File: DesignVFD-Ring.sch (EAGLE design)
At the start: 30 parts, among them IC1 LMR64010XMF/NOPB, IC2 LM340S-05, U1 MAX6920AWP+, U2 LM1084IS-5.0, U3 TPS76325DBVT

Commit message: Initial layout complete
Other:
- moved on the sheet: JP1
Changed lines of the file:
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@@
 <sheet>
 <plain>
-<text x="60.96" y="101.6" size="1.778" layer="91">Ribbon Cable for Ring</text>
+<text x="7.62" y="129.54" size="1.778" layer="91">Ribbon Cable for Ring</text>
 <text x="-73.66" y="246.38" size="6.4516" layer="91">TODO sort Caps</text>
 <text x="73.66" y="332.74" size="6.4516" layer="91">Batt to 12V</text>
@@
 </plain>
 <instances>
-<instance part="JP1" gate="A" x="76.2" y="93.98" smashed="yes" rot="R90">
-<attribute name="NAME" x="65.405" y="87.63" size="1.778" layer="95"/>
-<attribute name="VALUE" x="86.36" y="87.63" size="1.778" layer="96" rot="R90"/>
+<instance part="JP1" gate="A" x="22.86" y="121.92" smashed="yes" rot="R90">
+<attribute name="NAME" x="12.065" y="115.57" size="1.778" layer="95"/>
+<attribute name="VALUE" x="33.02" y="115.57" size="1.778" layer="96" rot="R90"/>
 </instance>
 <instance part="IC1" gate="G$1" x="17.78" y="182.88" smashed="yes">
@@
 <segment>
 <pinref part="JP1" gate="A" pin="1"/>
-<wire x1="68.58" y1="91.44" x2="68.58" y2="76.2" width="0.1524" layer="91"/>
-<label x="68.58" y="76.2" size="1.778" layer="95" rot="R90"/>
+<wire x1="15.24" y1="119.38" x2="15.24" y2="104.14" width="0.1524" layer="91"/>
+<label x="15.24" y="104.14" size="1.778" layer="95" rot="R90"/>
 </segment>
 <segment>
 <pinref part="JP1" gate="A" pin="3"/>
-<wire x1="73.66" y1="91.44" x2="73.66" y2="76.2" width="0.1524" layer="91"/>
-<label x="73.66" y="76.2" size="1.778" layer="95" rot="R90"/>
+<wire x1="20.32" y1="119.38" x2="20.32" y2="104.14" width="0.1524" layer="91"/>
+<label x="20.32" y="104.14" size="1.778" layer="95" rot="R90"/>
 </segment>
 <segment>
 <pinref part="JP1" gate="A" pin="5"/>
-<wire x1="78.74" y1="91.44" x2="78.74" y2="76.2" width="0.1524" layer="91"/>
-<label x="78.74" y="76.2" size="1.778" layer="95" rot="R90"/>
+<wire x1="25.4" y1="119.38" x2="25.4" y2="104.14" width="0.1524" layer="91"/>
+<label x="25.4" y="104.14" size="1.778" layer="95" rot="R90"/>
 </segment>
 <segment>
 <pinref part="JP1" gate="A" pin="7"/>
-<wire x1="83.82" y1="91.44" x2="83.82" y2="76.2" width="0.1524" layer="91"/>
-<label x="83.82" y="76.2" size="1.778" layer="95" rot="R90"/>
+<wire x1="30.48" y1="119.38" x2="30.48" y2="104.14" width="0.1524" layer="91"/>
+<label x="30.48" y="104.14" size="1.778" layer="95" rot="R90"/>
 </segment>
 <segment>
@@
 <segment>
 <pinref part="JP1" gate="A" pin="2"/>
-<wire x1="71.12" y1="91.44" x2="71.12" y2="76.2" width="0.1524" layer="91"/>
-<label x="71.12" y="76.2" size="1.778" layer="95" rot="R90"/>
+<wire x1="17.78" y1="119.38" x2="17.78" y2="104.14" width="0.1524" layer="91"/>
+<label x="17.78" y="104.14" size="1.778" layer="95" rot="R90"/>
 </segment>
 <segment>
@@
 <segment>
 <pinref part="JP1" gate="A" pin="4"/>
-<wire x1="76.2" y1="91.44" x2="76.2" y2="76.2" width="0.1524" layer="91"/>
-<label x="76.2" y="76.2" size="1.778" layer="95" rot="R90"/>
+<wire x1="22.86" y1="119.38" x2="22.86" y2="104.14" width="0.1524" layer="91"/>
+<label x="22.86" y="104.14" size="1.778" layer="95" rot="R90"/>
 </segment>
 <segment>
@@
 <segment>
 <pinref part="JP1" gate="A" pin="6"/>
-<wire x1="81.28" y1="91.44" x2="81.28" y2="76.2" width="0.1524" layer="91"/>
-<label x="81.28" y="76.2" size="1.778" layer="95" rot="R90"/>
-</segment>
-<segment>
+<wire x1="27.94" y1="119.38" x2="27.94" y2="104.14" width="0.1524" layer="91"/>
+<label x="27.94" y="104.14" size="1.778" layer="95" rot="R90"/>
+</segment>
+<segment>

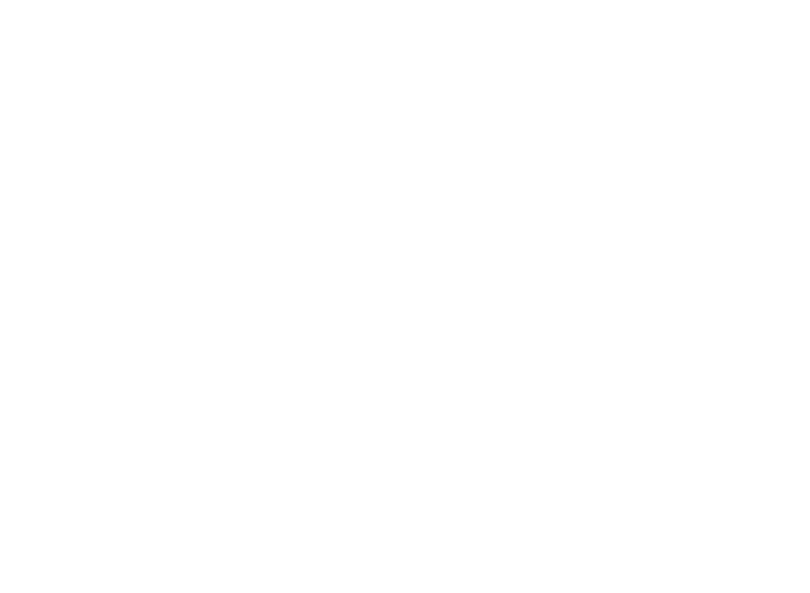
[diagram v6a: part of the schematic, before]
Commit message: added lumini ring
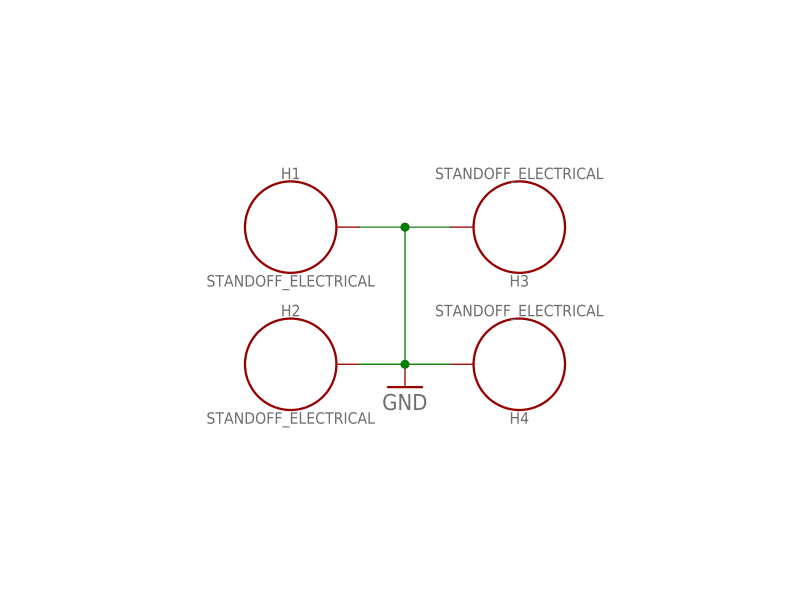
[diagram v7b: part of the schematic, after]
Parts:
- added H1, H2, H3, H4: STANDOFF_ELECTRICAL, SparkFun-Hardware:STANDOFF_ELECTRICAL
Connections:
- net GND: now also H1.P$1, H2.P$1, H3.P$1, H4.P$1
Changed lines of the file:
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@@
 <layer number="112" name="tSilk" color="7" fill="1" visible="no" active="yes"/>
 <layer number="113" name="ReferenceLS" color="7" fill="1" visible="no" active="no"/>
+<layer number="114" name="Badge_Outline" color="7" fill="1" visible="no" active="no"/>
+<layer number="115" name="ReferenceISLANDS" color="7" fill="1" visible="no" active="no"/>
 <layer number="116" name="Patch_BOT" color="9" fill="4" visible="no" active="yes"/>
 <layer number="118" name="Rect_Pads" color="7" fill="1" visible="no" active="no"/>
@@
 <part name="+3V4" library="supply1" library_urn="urn:adsk.eagle:library:371" deviceset="+3V3" device=""/>
 <part name="P+10" library="supply1" library_urn="urn:adsk.eagle:library:371" deviceset="+5V" device=""/>
+<part name="H1" library="SparkFun-Hardware" deviceset="STANDOFF_ELECTRICAL" device=""/>
+<part name="H2" library="SparkFun-Hardware" deviceset="STANDOFF_ELECTRICAL" device=""/>
+<part name="H3" library="SparkFun-Hardware" deviceset="STANDOFF_ELECTRICAL" device=""/>
+<part name="H4" library="SparkFun-Hardware" deviceset="STANDOFF_ELECTRICAL" device=""/>
+<part name="GND3" library="supply1" library_urn="urn:adsk.eagle:library:371" deviceset="GND" device=""/>
 </parts>
 <sheets>
@@
 <attribute name="VALUE" x="53.34" y="71.12" size="1.778" layer="96"/>
 </instance>
+<instance part="H1" gate="G$1" x="104.14" y="66.04" smashed="yes">
+<attribute name="NAME" x="104.14" y="71.374" size="1.27" layer="95" font="vector" align="bottom-center"/>
+<attribute name="VALUE" x="104.14" y="60.706" size="1.27" layer="96" font="vector" rot="R180" align="bottom-center"/>
+</instance>
+<instance part="H2" gate="G$1" x="104.14" y="50.8" smashed="yes">
+<attribute name="NAME" x="104.14" y="56.134" size="1.27" layer="95" font="vector" align="bottom-center"/>
+<attribute name="VALUE" x="104.14" y="45.466" size="1.27" layer="96" font="vector" rot="R180" align="bottom-center"/>
+</instance>
+<instance part="H3" gate="G$1" x="129.54" y="66.04" smashed="yes" rot="R180">
+<attribute name="NAME" x="129.54" y="60.706" size="1.27" layer="95" font="vector" rot="R180" align="bottom-center"/>
+<attribute name="VALUE" x="129.54" y="71.374" size="1.27" layer="96" font="vector" align="bottom-center"/>
+</instance>
+<instance part="H4" gate="G$1" x="129.54" y="50.8" smashed="yes" rot="R180">
+<attribute name="NAME" x="129.54" y="45.466" size="1.27" layer="95" font="vector" rot="R180" align="bottom-center"/>
+<attribute name="VALUE" x="129.54" y="56.134" size="1.27" layer="96" font="vector" align="bottom-center"/>
+</instance>
+<instance part="GND3" gate="1" x="116.84" y="48.26" smashed="yes">
+<attribute name="VALUE" x="114.3" y="45.72" size="1.778" layer="96"/>
+</instance>
 </instances>
 <busses>
@@
 <junction x="53.34" y="63.5"/>
 </segment>
+<segment>
+<pinref part="H1" gate="G$1" pin="P$1"/>
+<pinref part="H3" gate="G$1" pin="P$1"/>
+<wire x1="111.76" y1="66.04" x2="116.84" y2="66.04" width="0.1524" layer="91"/>
+<pinref part="H4" gate="G$1" pin="P$1"/>
+<pinref part="H2" gate="G$1" pin="P$1"/>
+<wire x1="116.84" y1="66.04" x2="121.92" y2="66.04" width="0.1524" layer="91"/>
+<wire x1="121.92" y1="50.8" x2="116.84" y2="50.8" width="0.1524" layer="91"/>
+<wire x1="116.84" y1="50.8" x2="111.76" y2="50.8" width="0.1524" layer="91"/>
+<wire x1="116.84" y1="66.04" x2="116.84" y2="50.8" width="0.1524" layer="91"/>
+<junction x="116.84" y="66.04"/>
+<junction x="116.84" y="50.8"/>
+<pinref part="GND3" gate="1" pin="GND"/>
+</segment>
 </net>

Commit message: about to repin IVL
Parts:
- removed H1, H2, H3, H4: STANDOFF_ELECTRICAL, SparkFun-Hardware:STANDOFF_ELECTRICAL
- added JP3: (no value), pinhead:PINHD-1X1
- added U$4: LUMINI3, FormE:LUMINI3
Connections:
- net +15V: now also JP3.1
- net GND: now also U$4.P$1; no longer H1.P$1, H2.P$1, H3.P$1, H4.P$1
- net T_CS2: now also U$3.3/CAN-TX/PWM; no longer U$3.5/PWM
- net T_MOSI2: now also U$3.5/PWM; no longer U$3.3/CAN-TX/PWM
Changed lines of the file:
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@@
 <part name="+3V4" library="supply1" library_urn="urn:adsk.eagle:library:371" deviceset="+3V3" device=""/>
 <part name="P+10" library="supply1" library_urn="urn:adsk.eagle:library:371" deviceset="+5V" device=""/>
-<part name="H1" library="SparkFun-Hardware" deviceset="STANDOFF_ELECTRICAL" device=""/>
-<part name="H2" library="SparkFun-Hardware" deviceset="STANDOFF_ELECTRICAL" device=""/>
-<part name="H3" library="SparkFun-Hardware" deviceset="STANDOFF_ELECTRICAL" device=""/>
-<part name="H4" library="SparkFun-Hardware" deviceset="STANDOFF_ELECTRICAL" device=""/>
 <part name="GND3" library="supply1" library_urn="urn:adsk.eagle:library:371" deviceset="GND" device=""/>
+<part name="U$4" library="FormE" deviceset="LUMINI3" device=""/>
+<part name="JP3" library="pinhead" library_urn="urn:adsk.eagle:library:325" deviceset="PINHD-1X1" device="" package3d_urn="urn:adsk.eagle:package:22485/2"/>
 </parts>
 <sheets>
@@
 <attribute name="VALUE" x="53.34" y="71.12" size="1.778" layer="96"/>
 </instance>
-<instance part="H1" gate="G$1" x="104.14" y="66.04" smashed="yes">
-<attribute name="NAME" x="104.14" y="71.374" size="1.27" layer="95" font="vector" align="bottom-center"/>
-<attribute name="VALUE" x="104.14" y="60.706" size="1.27" layer="96" font="vector" rot="R180" align="bottom-center"/>
-</instance>
-<instance part="H2" gate="G$1" x="104.14" y="50.8" smashed="yes">
-<attribute name="NAME" x="104.14" y="56.134" size="1.27" layer="95" font="vector" align="bottom-center"/>
-<attribute name="VALUE" x="104.14" y="45.466" size="1.27" layer="96" font="vector" rot="R180" align="bottom-center"/>
-</instance>
-<instance part="H3" gate="G$1" x="129.54" y="66.04" smashed="yes" rot="R180">
-<attribute name="NAME" x="129.54" y="60.706" size="1.27" layer="95" font="vector" rot="R180" align="bottom-center"/>
-<attribute name="VALUE" x="129.54" y="71.374" size="1.27" layer="96" font="vector" align="bottom-center"/>
-</instance>
-<instance part="H4" gate="G$1" x="129.54" y="50.8" smashed="yes" rot="R180">
-<attribute name="NAME" x="129.54" y="45.466" size="1.27" layer="95" font="vector" rot="R180" align="bottom-center"/>
-<attribute name="VALUE" x="129.54" y="56.134" size="1.27" layer="96" font="vector" align="bottom-center"/>
-</instance>
 <instance part="GND3" gate="1" x="116.84" y="48.26" smashed="yes">
 <attribute name="VALUE" x="114.3" y="45.72" size="1.778" layer="96"/>
+</instance>
+<instance part="U$4" gate="G$1" x="124.46" y="50.8" smashed="yes"/>
+<instance part="JP3" gate="G$1" x="-10.16" y="335.28" smashed="yes" rot="MR0">
+<attribute name="NAME" x="-3.81" y="338.455" size="1.778" layer="95" rot="MR0"/>
+<attribute name="VALUE" x="-3.81" y="330.2" size="1.778" layer="96" rot="MR0"/>
 </instance>
 </instances>
@@
 </segment>
 <segment>
-<pinref part="H1" gate="G$1" pin="P$1"/>
-<pinref part="H3" gate="G$1" pin="P$1"/>
-<wire x1="111.76" y1="66.04" x2="116.84" y2="66.04" width="0.1524" layer="91"/>
-<pinref part="H4" gate="G$1" pin="P$1"/>
-<pinref part="H2" gate="G$1" pin="P$1"/>
-<wire x1="116.84" y1="66.04" x2="121.92" y2="66.04" width="0.1524" layer="91"/>
-<wire x1="121.92" y1="50.8" x2="116.84" y2="50.8" width="0.1524" layer="91"/>
-<wire x1="116.84" y1="50.8" x2="111.76" y2="50.8" width="0.1524" layer="91"/>
-<wire x1="116.84" y1="66.04" x2="116.84" y2="50.8" width="0.1524" layer="91"/>
-<junction x="116.84" y="66.04"/>
-<junction x="116.84" y="50.8"/>
 <pinref part="GND3" gate="1" pin="GND"/>
+<pinref part="U$4" gate="G$1" pin="P$1"/>
+<wire x1="119.38" y1="50.8" x2="116.84" y2="50.8" width="0.1524" layer="91"/>
 </segment>
 </net>
@@
 <wire x1="15.24" y1="335.28" x2="10.16" y2="335.28" width="0.1524" layer="91"/>
 <junction x="10.16" y="335.28"/>
+<pinref part="JP3" gate="G$1" pin="1"/>
+<wire x1="-7.62" y1="335.28" x2="5.08" y2="335.28" width="0.1524" layer="91"/>
+<junction x="5.08" y="335.28"/>
 </segment>
 <segment>
@@
 </segment>
 <segment>
+<pinref part="U$3" gate="G$1" pin="3/CAN-TX/PWM"/>
+<wire x1="0" y1="63.5" x2="-12.7" y2="63.5" width="0.1524" layer="91"/>
+<label x="-12.7" y="63.5" size="1.778" layer="95"/>
+</segment>
+</net>
+<net name="T_MOSI" class="0">
+<segment>
+<pinref part="JP1" gate="A" pin="4"/>
+<wire x1="22.86" y1="119.38" x2="22.86" y2="104.14" width="0.1524" layer="91"/>
+<label x="22.86" y="104.14" size="1.778" layer="95" rot="R90"/>
+</segment>
+<segment>
+<pinref part="U$3" gate="G$1" pin="11/MOSI"/>
+<wire x1="0" y1="43.18" x2="-12.7" y2="43.18" width="0.1524" layer="91"/>
+<label x="-12.7" y="43.18" size="1.778" layer="95"/>
+</segment>
+</net>
+<net name="T_SCK" class="0">
+<segment>
+<pinref part="JP1" gate="A" pin="6"/>
+<wire x1="27.94" y1="119.38" x2="27.94" y2="104.14" width="0.1524" layer="91"/>
+<label x="27.94" y="104.14" size="1.778" layer="95" rot="R90"/>
+</segment>
+<segment>
+<pinref part="U$3" gate="G$1" pin="13/SCK/LED"/>
+<wire x1="0" y1="38.1" x2="-12.7" y2="38.1" width="0.1524" layer="91"/>
+<label x="-12.7" y="38.1" size="1.778" layer="95"/>
+</segment>
+</net>
+<net name="T_SCK2" class="0">
+<segment>
+<pinref part="U1" gate="G$1" pin="CLK"/>
+<wire x1="198.12" y1="93.98" x2="185.42" y2="93.98" width="0.1524" layer="91"/>
+<label x="185.42" y="93.98" size="1.778" layer="95"/>
+</segment>
+<segment>
+<pinref part="U$3" gate="G$1" pin="1/TX1/T"/>
+<wire x1="0" y1="68.58" x2="-12.7" y2="68.58" width="0.1524" layer="91"/>
+<label x="-12.7" y="68.58" size="1.778" layer="95"/>
+</segment>
+</net>
+<net name="T_MOSI2" class="0">
+<segment>
+<pinref part="U1" gate="G$1" pin="DIN"/>
+<wire x1="198.12" y1="91.44" x2="185.42" y2="91.44" width="0.1524" layer="91"/>
+<label x="185.42" y="91.44" size="1.778" layer="95"/>
+</segment>
+<segment>
 <pinref part="U$3" gate="G$1" pin="5/PWM"/>
 <wire x1="0" y1="58.42" x2="-12.7" y2="58.42" width="0.1524" layer="91"/>
@@
 </segment>
 </net>
-<net name="T_MOSI" class="0">
-<segment>
-<pinref part="JP1" gate="A" pin="4"/>
-<wire x1="22.86" y1="119.38" x2="22.86" y2="104.14" width="0.1524" layer="91"/>
-<label x="22.86" y="104.14" size="1.778" layer="95" rot="R90"/>
-</segment>
-<segment>
-<pinref part="U$3" gate="G$1" pin="11/MOSI"/>
-<wire x1="0" y1="43.18" x2="-12.7" y2="43.18" width="0.1524" layer="91"/>
-<label x="-12.7" y="43.18" size="1.778" layer="95"/>
-</segment>
-</net>
-<net name="T_SCK" class="0">
-<segment>
-<pinref part="JP1" gate="A" pin="6"/>
-<wire x1="27.94" y1="119.38" x2="27.94" y2="104.14" width="0.1524" layer="91"/>
-<label x="27.94" y="104.14" size="1.778" layer="95" rot="R90"/>
-</segment>
-<segment>
-<pinref part="U$3" gate="G$1" pin="13/SCK/LED"/>
-<wire x1="0" y1="38.1" x2="-12.7" y2="38.1" width="0.1524" layer="91"/>
-<label x="-12.7" y="38.1" size="1.778" layer="95"/>
-</segment>
-</net>
-<net name="T_SCK2" class="0">
-<segment>
-<pinref part="U1" gate="G$1" pin="CLK"/>
-<wire x1="198.12" y1="93.98" x2="185.42" y2="93.98" width="0.1524" layer="91"/>
-<label x="185.42" y="93.98" size="1.778" layer="95"/>
-</segment>
-<segment>
-<pinref part="U$3" gate="G$1" pin="1/TX1/T"/>
-<wire x1="0" y1="68.58" x2="-12.7" y2="68.58" width="0.1524" layer="91"/>
-<label x="-12.7" y="68.58" size="1.778" layer="95"/>
-</segment>
-</net>
-<net name="T_MOSI2" class="0">
-<segment>
-<pinref part="U1" gate="G$1" pin="DIN"/>
-<wire x1="198.12" y1="91.44" x2="185.42" y2="91.44" width="0.1524" layer="91"/>
-<label x="185.42" y="91.44" size="1.778" layer="95"/>
-</segment>
-<segment>
-<pinref part="U$3" gate="G$1" pin="3/CAN-TX/PWM"/>
-<wire x1="0" y1="63.5" x2="-12.7" y2="63.5" width="0.1524" layer="91"/>
-<label x="-12.7" y="63.5" size="1.778" layer="95"/>
-</segment>
-</net>
